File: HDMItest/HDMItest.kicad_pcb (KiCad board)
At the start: 2 copper layers, 40.1 x 29 mm, 4 parts, among them J1 HDMI_A, J2 Conn_02x06_Odd_Even

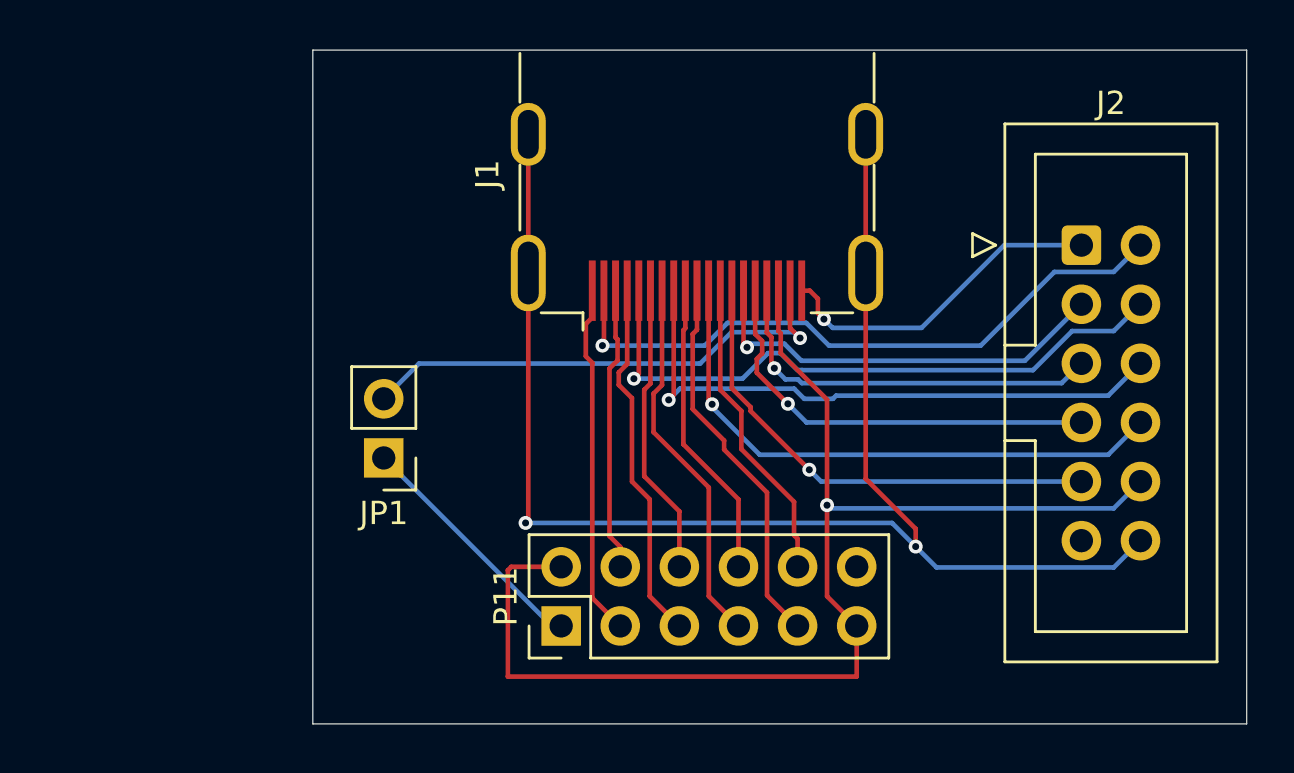
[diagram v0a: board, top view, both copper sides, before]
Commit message: new HDMI test with re-driver
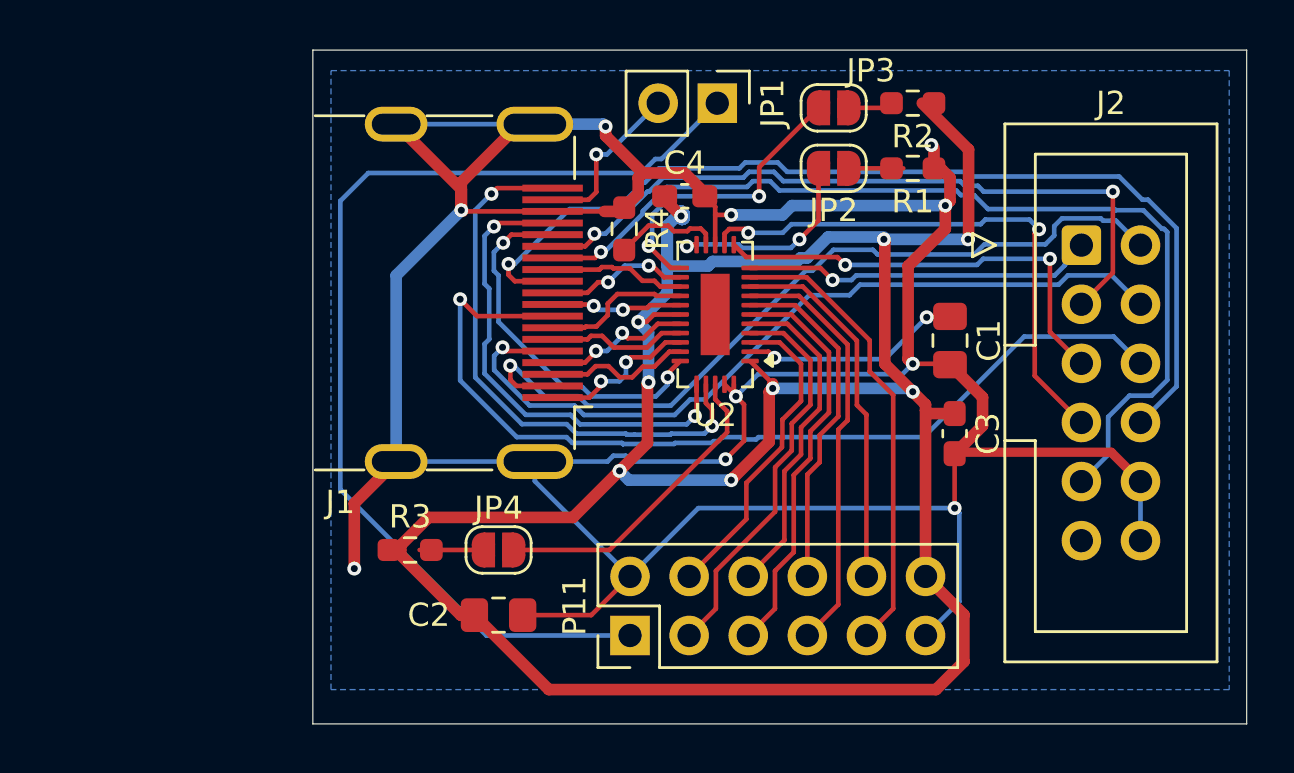
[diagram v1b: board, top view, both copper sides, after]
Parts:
- added C1: 4u7, Capacitor_SMD:C_0805_2012Metric_Pad1.18x1.45mm_HandSolder, F.Cu at (146.0, 93.0)
- added C2: 22u, Capacitor_SMD:C_0805_2012Metric_Pad1.18x1.45mm_HandSolder, F.Cu at (126.6, 104.8)
- added C3: 100n, Capacitor_SMD:C_0603_1608Metric_Pad1.08x0.95mm_HandSolder, F.Cu at (146.2, 97.0)
- added C4: 100n, Capacitor_SMD:C_0603_1608Metric_Pad1.08x0.95mm_HandSolder, F.Cu at (134.6, 86.8)
- added JP2: SolderJumper_2_Open, Jumper:SolderJumper-2_P1.3mm_Open_RoundedPad1.0x1.5mm, F.Cu at (141.0, 85.6)
- added JP3: SolderJumper_2_Open, Jumper:SolderJumper-2_P1.3mm_Open_RoundedPad1.0x1.5mm, F.Cu at (141.0, 83.0)
- added JP4: SolderJumper_2_Open, Jumper:SolderJumper-2_P1.3mm_Open_RoundedPad1.0x1.5mm, F.Cu at (126.6, 102.0)
- added R1: 1k, Resistor_SMD:R_0603_1608Metric_Pad0.98x0.95mm_HandSolder, F.Cu at (144.4, 85.6)
- added R2: 1k, Resistor_SMD:R_0603_1608Metric_Pad0.98x0.95mm_HandSolder, F.Cu at (144.4, 82.8)
- added R3: 1k, Resistor_SMD:R_0603_1608Metric_Pad0.98x0.95mm_HandSolder, F.Cu at (122.8, 102.0)
- added R4: 1k, Resistor_SMD:R_0603_1608Metric_Pad0.98x0.95mm_HandSolder, F.Cu at (132.0, 88.2)
- added U2: ~, Package_DFN_QFN:Diodes_ZL32_TQFN-32-1EP_3x6mm_P0.4mm_EP1.25x3.5mm, F.Cu at (135.9, 91.9)
- moved JP1 20.9 mm to (136.0, 82.8), turned to -90 degrees
- moved J1 10.1 mm to (125.6, 91.0), turned to 180 degrees
- moved P11 2.99 mm to (132.2, 105.7)
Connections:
- J1 pad SH: Net-(J2-Pin_12) -> GND
- J2 pad 1: Net-(J1-HPD) -> Net-(J2-Pin_1)
- J2 pad 12: Net-(J2-Pin_12) -> GND
- J2 pad 5: Net-(J1-SDA) -> Net-(J2-Pin_5)
- J2 pad 7: Net-(J1-SCL) -> Net-(J2-Pin_7)
- P11 pad 10: Net-(J1-CK-) -> Net-(P11-HSYNC)
- P11 pad 12: unconnected-(P11-V33-Pad12) -> Net-(P11-V33)
- P11 pad 3: Net-(J1-D2+) -> Net-(P11-R)
- P11 pad 4: Net-(J1-D2-) -> Net-(P11-RI)
- P11 pad 5: Net-(J1-D1+) -> Net-(P11-G)
- P11 pad 6: Net-(J1-D1-) -> Net-(P11-GI)
- P11 pad 7: Net-(J1-D0+) -> Net-(P11-B)
- P11 pad 8: Net-(J1-D0-) -> Net-(P11-BI)
- P11 pad 9: Net-(J1-CK+) -> Net-(P11-VSYNC)
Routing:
- net Net-(P11-V33): track 0.00 -> 115.8 mm, vias 0 -> 9
- net GND: track 53.9 -> 154.6 mm, vias 1 -> 10
- net Net-(J2-Pin_12): track 63.1 -> 0.00 mm, vias 2 -> 0
- net Net-(JP1-A): track 10.6 -> 45.4 mm
- net Net-(J2-Pin_7): track 0.00 -> 23.8 mm, vias 0 -> 2
- net Net-(J1-CEC): track 21.0 -> 41.6 mm
- net Net-(P11-VSYNC): track 0.00 -> 19.8 mm
- net Net-(J2-Pin_5): track 0.00 -> 19.1 mm, vias 0 -> 2
- net Net-(P11-B): track 0.00 -> 18.3 mm
- net Net-(J1-CKS): track 24.9 -> 43.1 mm
- net Net-(P11-G): track 0.00 -> 17.7 mm
- net Net-(P11-R): track 0.00 -> 17.1 mm
- net Net-(P11-HSYNC): track 0.00 -> 15.9 mm
- net Net-(J2-Pin_1): track 0.00 -> 15.2 mm, vias 0 -> 1
- net Net-(P11-BI): track 0.00 -> 14.9 mm
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- added copper zone on B.Cu, net GND

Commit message: new HDMI adapter with AC coupling
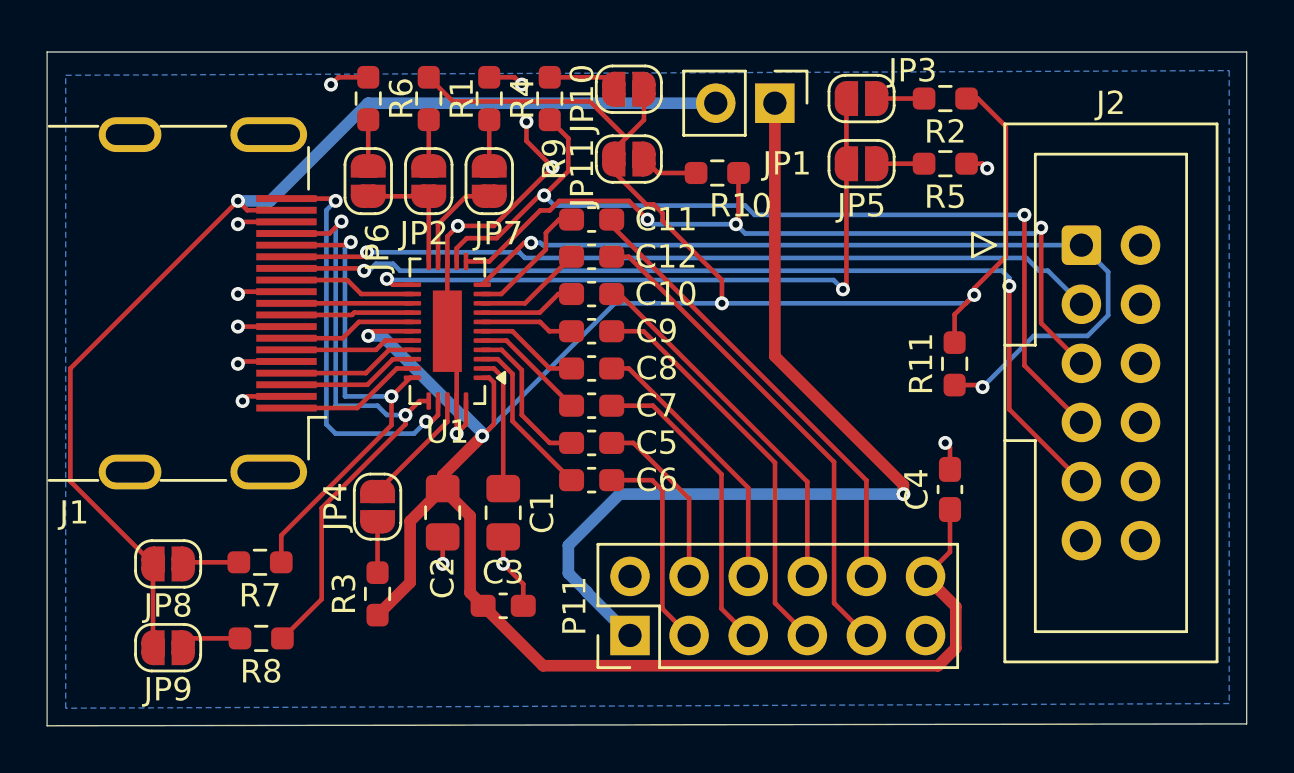
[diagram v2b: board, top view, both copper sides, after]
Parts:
- removed U2: ~, Package_DFN_QFN:Diodes_ZL32_TQFN-32-1EP_3x6mm_P0.4mm_EP1.25x3.5mm
- added C10: 100n, Capacitor_SMD:C_0603_1608Metric_Pad1.08x0.95mm_HandSolder, F.Cu at (130.6, 91.0)
- added C11: 100n, Capacitor_SMD:C_0603_1608Metric_Pad1.08x0.95mm_HandSolder, F.Cu at (130.6, 87.8)
- added C12: 100n, Capacitor_SMD:C_0603_1608Metric_Pad1.08x0.95mm_HandSolder, F.Cu at (130.6, 89.4)
- added C5: 100n, Capacitor_SMD:C_0603_1608Metric_Pad1.08x0.95mm_HandSolder, F.Cu at (130.6, 97.4)
- added C6: 100n, Capacitor_SMD:C_0603_1608Metric_Pad1.08x0.95mm_HandSolder, F.Cu at (130.6, 99.0)
- added C7: 100n, Capacitor_SMD:C_0603_1608Metric_Pad1.08x0.95mm_HandSolder, F.Cu at (130.6, 95.8)
- added C8: 100n, Capacitor_SMD:C_0603_1608Metric_Pad1.08x0.95mm_HandSolder, F.Cu at (130.6, 94.2)
- added C9: 100n, Capacitor_SMD:C_0603_1608Metric_Pad1.08x0.95mm_HandSolder, F.Cu at (130.6, 92.6)
- added JP10: SolderJumper_2_Open, Jumper:SolderJumper-2_P1.3mm_Open_RoundedPad1.0x1.5mm, F.Cu at (132.2, 82.2)
- added JP11: SolderJumper_2_Open, Jumper:SolderJumper-2_P1.3mm_Open_RoundedPad1.0x1.5mm, F.Cu at (132.2, 85.2)
- added JP5: SolderJumper_2_Open, Jumper:SolderJumper-2_P1.3mm_Open_RoundedPad1.0x1.5mm, F.Cu at (142.2, 85.4)
- added JP6: SolderJumper_2_Open, Jumper:SolderJumper-2_P1.3mm_Open_RoundedPad1.0x1.5mm, F.Cu at (121.0, 86.2)
- added JP7: SolderJumper_2_Open, Jumper:SolderJumper-2_P1.3mm_Open_RoundedPad1.0x1.5mm, F.Cu at (126.2, 86.2)
- added JP8: SolderJumper_2_Open, Jumper:SolderJumper-2_P1.3mm_Open_RoundedPad1.0x1.5mm, F.Cu at (112.4, 102.6)
- added JP9: SolderJumper_2_Open, Jumper:SolderJumper-2_P1.3mm_Open_RoundedPad1.0x1.5mm, F.Cu at (112.4, 106.2)
- added R10: 4k7, Resistor_SMD:R_0603_1608Metric_Pad0.98x0.95mm_HandSolder, F.Cu at (136.0, 85.8)
- added R11: 4k7, Resistor_SMD:R_0603_1608Metric_Pad0.98x0.95mm_HandSolder, F.Cu at (146.2, 94.0)
- added R5: 1k, Resistor_SMD:R_0603_1608Metric_Pad0.98x0.95mm_HandSolder, F.Cu at (145.8, 85.4)
- added R6: 1k, Resistor_SMD:R_0603_1608Metric_Pad0.98x0.95mm_HandSolder, F.Cu at (121.0, 82.6)
- added R7: 2k2, Resistor_SMD:R_0603_1608Metric_Pad0.98x0.95mm_HandSolder, F.Cu at (116.3, 102.5)
- added R8: 2k2, Resistor_SMD:R_0603_1608Metric_Pad0.98x0.95mm_HandSolder, F.Cu at (116.4, 105.8)
- added R9: 4k7, Resistor_SMD:R_0603_1608Metric_Pad0.98x0.95mm_HandSolder, F.Cu at (128.8, 82.6)
- added U1: ~, Package_DFN_QFN:Diodes_ZL32_TQFN-32-1EP_3x6mm_P0.4mm_EP1.25x3.5mm, F.Cu at (124.4, 92.6)
- moved R1 21.0 mm to (123.6, 82.6), turned to -90 degrees
- moved C3 20.8 mm to (126.8, 104.4), turned to 0 degrees
- moved C1 20.6 mm to (126.8, 100.4)
- moved JP2 17.4 mm to (123.6, 86.2), turned to -90 degrees
- moved C4 17.0 mm to (146.0, 99.4), turned to 90 degrees
- moved J1 11.4 mm to (114.2, 91.4)
- moved R4 8.06 mm to (126.2, 82.6)
- moved JP4 5.52 mm to (121.4, 100.1), turned to 90 degrees
- moved C2 5.01 mm to (124.2, 100.4), turned to -90 degrees
- moved JP1 2.47 mm to (138.5, 82.8)
- moved R3 2.35 mm to (121.4, 103.9), turned to 90 degrees
- moved R2 1.41 mm to (145.8, 82.6)
- moved JP3 1.26 mm to (142.2, 82.6)
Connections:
- C2 pad 1: Net-(P11-V33) -> Net-(JP10-B)
- C3 pad 1: Net-(P11-V33) -> Net-(JP10-B)
- C4 pad 1: Net-(P11-V33) -> Net-(JP10-B)
- J1 pad 11: Net-(J1-CKS) -> GND
- J1 pad 2: Net-(J1-D2S) -> GND
- J1 pad 5: Net-(J1-D1S) -> GND
- J1 pad 8: Net-(J1-D0S) -> GND
- J2 pad 10: GND -> unconnected-(J2-Pin_10-Pad10)
- J2 pad 11: unconnected-(J2-Pin_11-Pad11) -> GND
- J2 pad 12: GND -> unconnected-(J2-Pin_12-Pad12)
- J2 pad 2: Net-(J1-D2S) -> unconnected-(J2-Pin_2-Pad2)
- J2 pad 4: Net-(J1-D1S) -> unconnected-(J2-Pin_4-Pad4)
- J2 pad 6: Net-(J1-D0S) -> unconnected-(J2-Pin_6-Pad6)
- J2 pad 8: Net-(J1-CKS) -> unconnected-(J2-Pin_8-Pad8)
- P11 pad 12: Net-(P11-V33) -> Net-(JP10-B)
- R1 pad 1: GND -> Net-(JP10-B)
- R2 pad 1: Net-(P11-V33) -> Net-(JP10-B)
- R3 pad 1: Net-(P11-V33) -> Net-(JP10-B)
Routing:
- net GND: track 154.6 -> 38.7 mm, vias 10 -> 15
- net Net-(P11-V33): track 115.8 -> 0.00 mm, vias 9 -> 0
- net Net-(JP10-B): track 0.00 -> 113.4 mm, vias 0 -> 4
- net Net-(J1-CKS): track 43.1 -> 0.00 mm, vias 1 -> 0
- net Net-(J1-+5V): track 7.21 -> 48.2 mm
- net Net-(J1-D0S): track 40.6 -> 0.00 mm, vias 1 -> 0
- net Net-(J1-D1S): track 34.9 -> 0.00 mm, vias 1 -> 0
- net Net-(J1-D2S): track 34.5 -> 0.00 mm, vias 1 -> 0
- net Net-(J2-Pin_1): track 15.2 -> 37.9 mm, vias 1 -> 2
- net Net-(J2-Pin_7): track 23.8 -> 40.2 mm
- net Net-(JP3-B): track 12.9 -> 29.3 mm
- net Net-(J2-Pin_5): track 19.1 -> 35.3 mm, vias 2 -> 3
- net Net-(JP4-B): track 13.5 -> 5.13 mm
- net Net-(P11-R): track 17.1 -> 9.07 mm
- net Net-(U1-RD2_N): track 0.00 -> 7.18 mm
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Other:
- board size 40.1 x 29 mm -> 51.5 x 29 mm
